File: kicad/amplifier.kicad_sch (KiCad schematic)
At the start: 2 parts, among them U6 AD8421

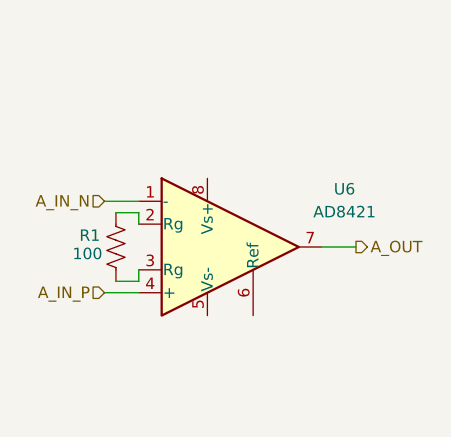
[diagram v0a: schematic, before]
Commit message: finish schematic for amp, and start routing (schematic isn't actually fully connected yet tho...)
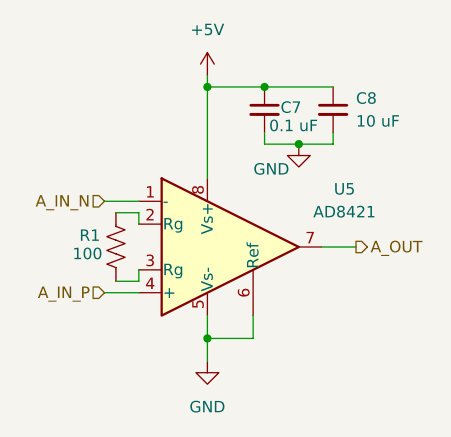
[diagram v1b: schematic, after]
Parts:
- added C7: 0.1 uF, Capacitor_SMD:C_0603_1608Metric, symbol Device:C_Small
- added C8: 10 uF, Capacitor_SMD:C_0805_2012Metric, symbol Device:C_Small
- R1: footprint (none) -> Resistor_SMD:R_0603_1608Metric
- U5: renamed from U6; footprint (none) -> Package_SO:MSOP-8_3x3mm_P0.65mm
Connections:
- net GND: now reaches U5.5 (Vs-)
- net GND: now also U5.6 (Ref), C7.2, C8.2
- net +5V: now reaches U5.8 (Vs+)
- net +5V: now also C7.1, C8.1

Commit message: make the component values more visible on pcb
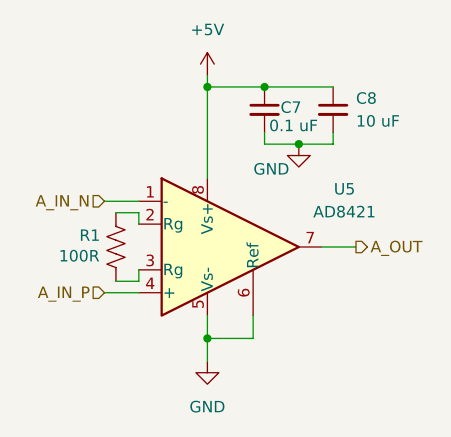
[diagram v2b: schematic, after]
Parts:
- R1: value 100 -> 100R
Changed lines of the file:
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@@
 			)
 		)
-		(property "Value" "100"
-			(at 124.714 104.902 0)
+		(property "Value" "100R"
+			(at 123.19 105.156 0)
 			(effects
 				(font

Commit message: slightly better routing
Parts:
- R1: value 100R -> 100
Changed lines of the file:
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@@
 			)
 		)
-		(property "Value" "100R"
-			(at 123.19 105.156 0)
+		(property "Value" "100"
+			(at 124.46 105.156 0)
 			(effects
 				(font
